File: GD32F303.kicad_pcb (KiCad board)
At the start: 2 copper layers, 0 parts

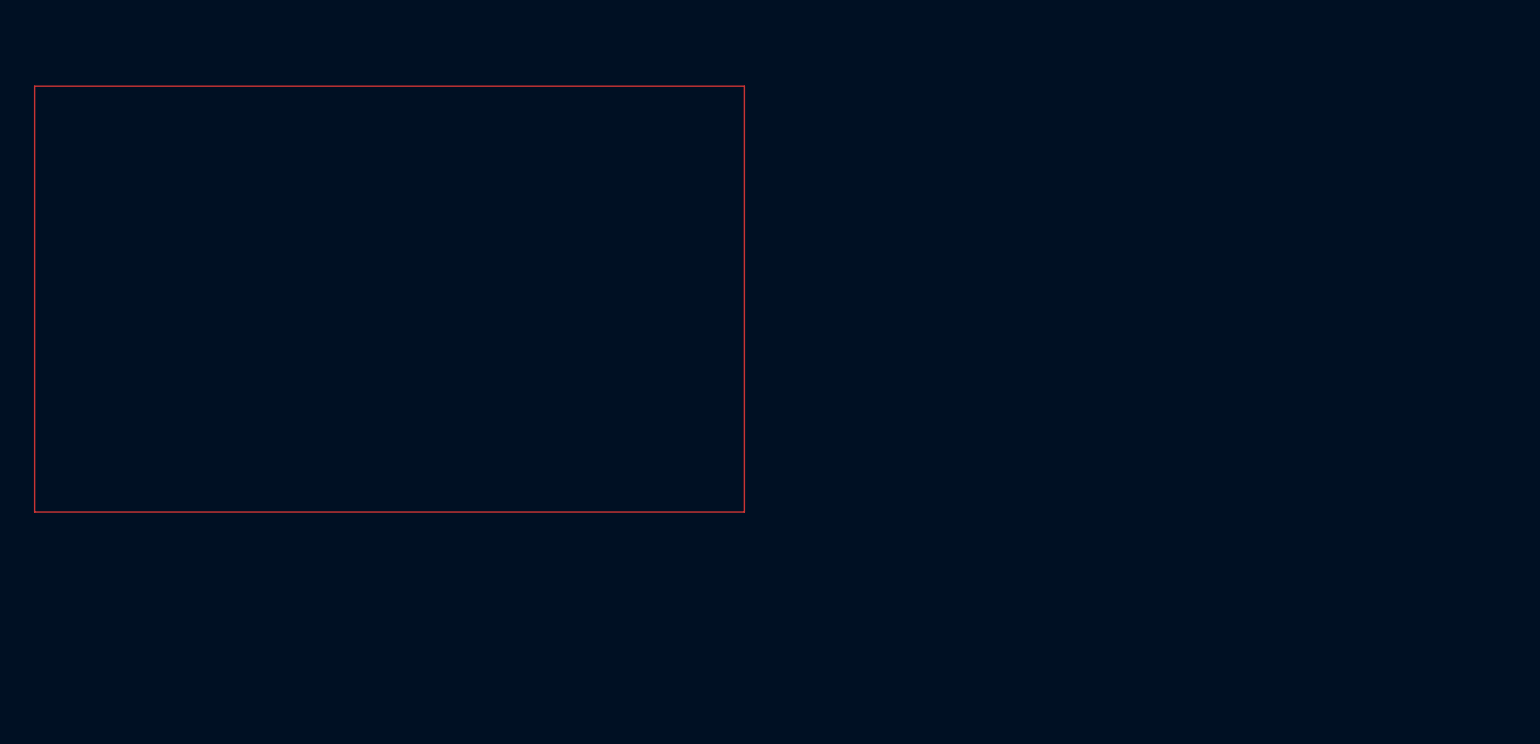
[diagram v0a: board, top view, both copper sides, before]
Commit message: 完成GD32F303控制板原理图与PCB设计
- 更新电源、CAN、RS232、RS485及电机通信子电路
- 切换并完善GD32F303VCT6核心原理图
- 新增PCB布局及所需符号、封装库文件
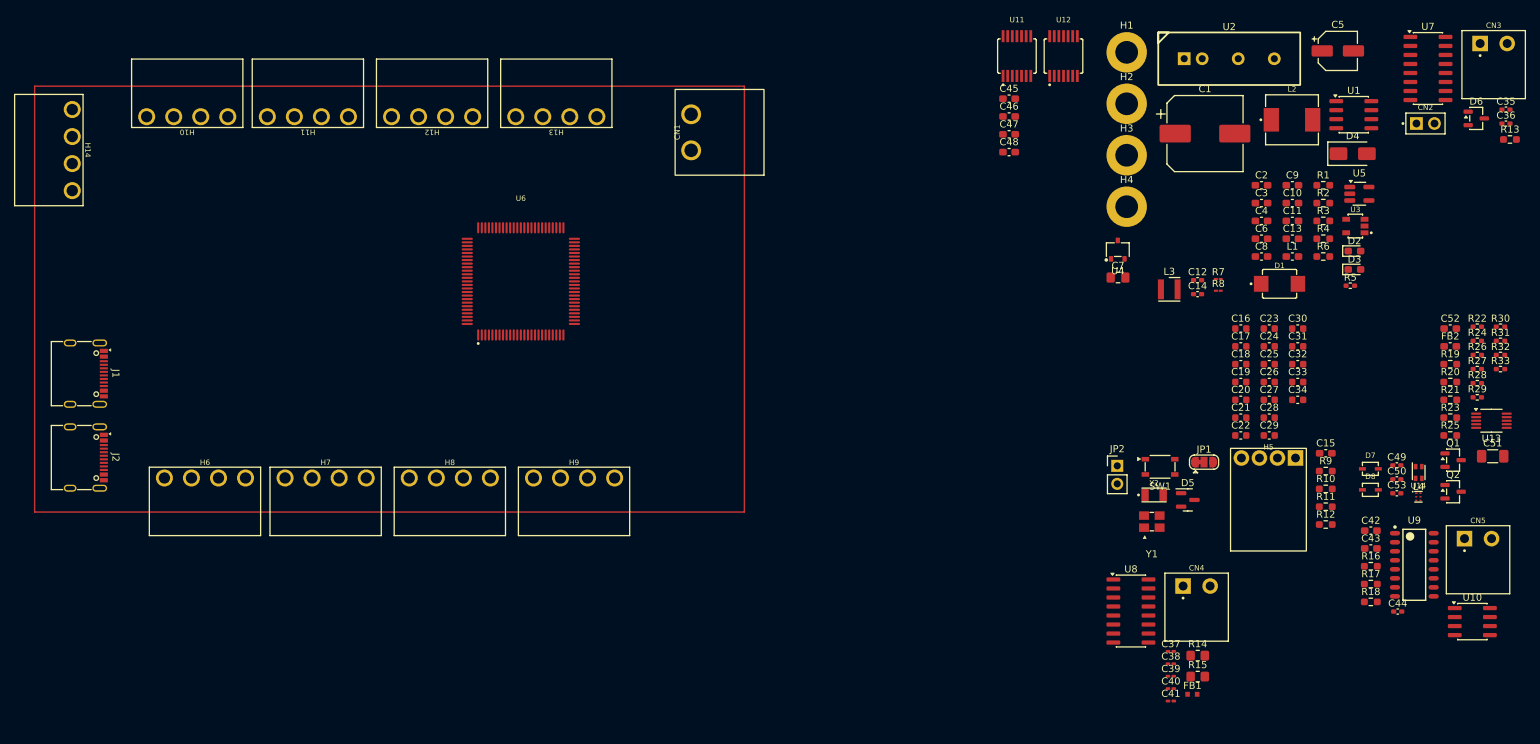
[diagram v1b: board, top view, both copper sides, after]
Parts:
- added C1: 470µF, Capacitor_SMD:CP_Elec_10x10.5, F.Cu at (250.4, 65.7)
- added C10: 100nF, Capacitor_SMD:C_0603_1608Metric_Pad1.08x0.95mm_HandSolder, F.Cu at (262.7, 75.5)
- added C11: 1nF, Capacitor_SMD:C_0603_1608Metric_Pad1.08x0.95mm_HandSolder, F.Cu at (262.7, 78.0)
- added C12: 100nF, Capacitor_SMD:C_0402_1005Metric_Pad0.74x0.62mm_HandSolder, F.Cu at (249.4, 86.3)
- added C13: 22uF, Capacitor_SMD:C_0603_1608Metric_Pad1.08x0.95mm_HandSolder, F.Cu at (262.7, 80.5)
- added C14: 100nF, Capacitor_SMD:C_0402_1005Metric_Pad0.74x0.62mm_HandSolder, F.Cu at (249.4, 88.3)
- added C15: 22pF, Capacitor_SMD:C_0603_1608Metric_Pad1.08x0.95mm_HandSolder, F.Cu at (267.4, 110.7)
- added C16: 100nF, Capacitor_SMD:C_0603_1608Metric, F.Cu at (255.4, 93.2)
- added C17: 100nF, Capacitor_SMD:C_0603_1608Metric, F.Cu at (255.4, 95.7)
- added C18: 100nF, Capacitor_SMD:C_0603_1608Metric, F.Cu at (255.4, 98.2)
- added C19: 100nF, Capacitor_SMD:C_0603_1608Metric, F.Cu at (255.4, 100.7)
- added C2: 10uF, Capacitor_SMD:C_0603_1608Metric_Pad1.08x0.95mm_HandSolder, F.Cu at (258.4, 73.0)
- added C20: 22pF, Capacitor_SMD:C_0603_1608Metric, F.Cu at (255.4, 103.2)
- added C21: 100nF, Capacitor_SMD:C_0603_1608Metric, F.Cu at (255.4, 105.7)
- added C22: 100nF, Capacitor_SMD:C_0603_1608Metric, F.Cu at (255.4, 108.2)
- added C23: 100nF, Capacitor_SMD:C_0603_1608Metric, F.Cu at (259.5, 93.2)
- added C24: 100nF, Capacitor_SMD:C_0603_1608Metric, F.Cu at (259.5, 95.7)
- added C25: 100nF, Capacitor_SMD:C_0603_1608Metric, F.Cu at (259.5, 98.2)
- added C26: 100nF, Capacitor_SMD:C_0603_1608Metric, F.Cu at (259.5, 100.7)
- added C27: 100nF, Capacitor_SMD:C_0603_1608Metric, F.Cu at (259.5, 103.2)
- added C28: 12pF, Capacitor_SMD:C_0603_1608Metric, F.Cu at (259.5, 105.7)
- added C29: 100nF, Capacitor_SMD:C_0603_1608Metric, F.Cu at (259.5, 108.2)
- added C3: 22pF, Capacitor_SMD:C_0603_1608Metric_Pad1.08x0.95mm_HandSolder, F.Cu at (258.4, 75.5)
- added C30: 100nF, Capacitor_SMD:C_0603_1608Metric, F.Cu at (263.5, 93.2)
- added C31: 12pF, Capacitor_SMD:C_0603_1608Metric, F.Cu at (263.5, 95.7)
- added C32: 100nF, Capacitor_SMD:C_0603_1608Metric, F.Cu at (263.5, 98.2)
- added C33: 10uF, Capacitor_SMD:C_0603_1608Metric, F.Cu at (263.5, 100.7)
- added C34: 100nF, Capacitor_SMD:C_0603_1608Metric, F.Cu at (263.5, 103.2)
- added C35: 100nF, Capacitor_SMD:C_0402_1005Metric_Pad0.74x0.62mm_HandSolder, F.Cu at (292.8, 62.3)
- added C36: 100nF, Capacitor_SMD:C_0402_1005Metric_Pad0.74x0.62mm_HandSolder, F.Cu at (292.8, 64.3)
- added C37: 100nF, Capacitor_SMD:C_0201_0603Metric_Pad0.64x0.40mm_HandSolder, F.Cu at (245.6, 138.6)
- added C38: 100nF, Capacitor_SMD:C_0201_0603Metric_Pad0.64x0.40mm_HandSolder, F.Cu at (245.6, 140.4)
- added C39: 100nF, Capacitor_SMD:C_0201_0603Metric_Pad0.64x0.40mm_HandSolder, F.Cu at (245.6, 142.1)
- added C4: 10uF, Capacitor_SMD:C_0603_1608Metric_Pad1.08x0.95mm_HandSolder, F.Cu at (258.4, 78.0)
- added C40: 100nF, Capacitor_SMD:C_0201_0603Metric_Pad0.64x0.40mm_HandSolder, F.Cu at (245.6, 143.9)
- added C41: 100nF, Capacitor_SMD:C_0201_0603Metric_Pad0.64x0.40mm_HandSolder, F.Cu at (245.6, 145.6)
- added C42: 0.1uF, Capacitor_SMD:C_0603_1608Metric_Pad1.08x0.95mm_HandSolder, F.Cu at (273.8, 121.6)
- added C43: 0.1uF, Capacitor_SMD:C_0603_1608Metric_Pad1.08x0.95mm_HandSolder, F.Cu at (273.8, 124.1)
- added C44: 100nF, Capacitor_SMD:C_0402_1005Metric_Pad0.74x0.62mm_HandSolder, F.Cu at (277.6, 133.0)
- added C45: 0.1uF, Capacitor_SMD:C_0603_1608Metric_Pad1.08x0.95mm_HandSolder, F.Cu at (222.8, 60.8)
- added C46: 0.1uF, Capacitor_SMD:C_0603_1608Metric_Pad1.08x0.95mm_HandSolder, F.Cu at (222.8, 63.3)
- added C47: 0.1uF, Capacitor_SMD:C_0603_1608Metric_Pad1.08x0.95mm_HandSolder, F.Cu at (222.8, 65.8)
- added C48: 0.1uF, Capacitor_SMD:C_0603_1608Metric_Pad1.08x0.95mm_HandSolder, F.Cu at (222.8, 68.3)
- added C49: 100nF, Capacitor_SMD:C_0402_1005Metric_Pad0.74x0.62mm_HandSolder, F.Cu at (277.4, 112.4)
- added C5: 220µF, Capacitor_SMD:CP_Elec_5x5.4, F.Cu at (269.1, 54.0)
- added C50: 100nF, Capacitor_SMD:C_0402_1005Metric_Pad0.74x0.62mm_HandSolder, F.Cu at (277.4, 114.4)
- added C51: 1nF, Capacitor_SMD:C_1206_3216Metric_Pad1.33x1.80mm_HandSolder, F.Cu at (290.9, 111.1)
- added C52: 10uF, Capacitor_SMD:C_0603_1608Metric_Pad1.08x0.95mm_HandSolder, F.Cu at (285.0, 93.2)
- added C53: 100nF, Capacitor_SMD:C_0402_1005Metric_Pad0.74x0.62mm_HandSolder, F.Cu at (277.4, 116.4)
- added C6: 10uF, Capacitor_SMD:C_0603_1608Metric_Pad1.08x0.95mm_HandSolder, F.Cu at (258.4, 80.5)
- added C7: 10uF, Capacitor_SMD:C_0805_2012Metric_Pad1.18x1.45mm_HandSolder, F.Cu at (238.1, 86.0)
- added C8: 1uF, Capacitor_SMD:C_0603_1608Metric_Pad1.08x0.95mm_HandSolder, F.Cu at (258.4, 83.0)
- added C9: 10uF, Capacitor_SMD:C_0603_1608Metric_Pad1.08x0.95mm_HandSolder, F.Cu at (262.7, 73.0)
- added CN1: DB2ERC-5.08-2P-GN, kicad_api_lib:DB2ERC-5.08-2P-GN, F.Cu at (178.0, 65.5)
- added CN2: PZ254-1-02-W-8.5, kicad_api_lib:PZ254-1-02-W-8.5, F.Cu at (281.5, 64.3)
- added CN3: WJ15EDGRC-3.81-2P, kicad_api_lib:WJ15EDGRC-3.81-2P, F.Cu at (291.1, 53.0)
- added CN4: WJ15EDGRC-3.81-2P, kicad_api_lib:WJ15EDGRC-3.81-2P, F.Cu at (249.2, 129.4)
- added CN5: WJ15EDGRC-3.81-2P, kicad_api_lib:WJ15EDGRC-3.81-2P, F.Cu at (288.9, 122.7)
- added D1: SMBJ24A, kicad_api_lib:SMBJ24A, F.Cu at (260.9, 86.8)
- added D2: LED, LED_SMD:LED_0603_1608Metric_Pad1.05x0.95mm_HandSolder, F.Cu at (271.5, 82.2)
- added D3: LED, LED_SMD:LED_0603_1608Metric_Pad1.05x0.95mm_HandSolder, F.Cu at (271.5, 84.8)
- added D4: SS34, Diode_SMD:D_SMA, F.Cu at (271.2, 68.5)
- added D5: BAT54CTA, kicad_api_lib:BAT54CTA, F.Cu at (248.0, 117.3)
- added D6: ESDA6V1L, Package_TO_SOT_SMD:SOT-23-3, F.Cu at (288.6, 63.5)
- added D7: SD03C, kicad_api_lib:SD03C, F.Cu at (273.7, 112.9)
- added D8: SD03C, kicad_api_lib:SD03C, F.Cu at (273.7, 115.9)
- added FB1: BLM18AG601SN1D, kicad_api_lib:BLM18AG601SN1D, F.Cu at (248.6, 144.7)
- added FB2: 100ohm@100MHz, Capacitor_SMD:C_0603_1608Metric_Pad1.08x0.95mm_HandSolder, F.Cu at (285.0, 95.7)
- added H1: MountingHole_Pad, MountingHole:MountingHole_3.2mm_M3_ISO7380_Pad, F.Cu at (239.4, 54.2)
- added H10: KF2EDGRM-3.81-4P, kicad_api_lib:KF2EDGRM-3.81-4P, F.Cu at (107.0, 63.3)
- added H11: KF2EDGRM-3.81-4P, kicad_api_lib:KF2EDGRM-3.81-4P, F.Cu at (124.0, 63.3)
- added H12: KF2EDGRM-3.81-4P, kicad_api_lib:KF2EDGRM-3.81-4P, F.Cu at (141.5, 63.3)
- added H13: KF2EDGRM-3.81-4P, kicad_api_lib:KF2EDGRM-3.81-4P, F.Cu at (159.0, 63.3)
- added H14: KF2EDGRM-3.81-4P, kicad_api_lib:KF2EDGRM-3.81-4P, F.Cu at (90.8, 68.0)
- added H2: MountingHole_Pad, MountingHole:MountingHole_3.2mm_M3_ISO7380_Pad, F.Cu at (239.4, 61.5)
- added H3: MountingHole_Pad, MountingHole:MountingHole_3.2mm_M3_ISO7380_Pad, F.Cu at (239.4, 68.7)
- added H4: MountingHole_Pad, MountingHole:MountingHole_3.2mm_M3_ISO7380_Pad, F.Cu at (239.4, 76.0)
- added H5: X9254WR-04-N0SN, kicad_api_lib:X9254WR-04-N0SN, F.Cu at (259.3, 111.4)
- added H6: KF2EDGRM-3.81-4P, kicad_api_lib:KF2EDGRM-3.81-4P, F.Cu at (109.5, 114.2)
- added H7: KF2EDGRM-3.81-4P, kicad_api_lib:KF2EDGRM-3.81-4P, F.Cu at (126.5, 114.2)
- added H8: KF2EDGRM-3.81-4P, kicad_api_lib:KF2EDGRM-3.81-4P, F.Cu at (144.0, 114.2)
- added H9: KF2EDGRM-3.81-4P, kicad_api_lib:KF2EDGRM-3.81-4P, F.Cu at (161.5, 114.2)
- added J1: TYPE-C-31-M-31, kicad_api_lib:TYPE-C 16PIN 2MD(073), F.Cu at (94.2, 99.5)
- added J2: TYPE-C 16PIN 2MD(073), kicad_api_lib:TYPE-C 16PIN 2MD(073), F.Cu at (94.2, 111.3)
- added JP1: SolderJumper_3_Bridged12, Jumper:SolderJumper-3_P1.3mm_Bridged12_RoundedPad1.0x1.5mm, F.Cu at (250.3, 112.0)
- added JP2: Jumper_2_Small_Open, Connector_PinHeader_2.54mm:PinHeader_1x02_P2.54mm_Vertical, F.Cu at (238.0, 112.5)
- added L1: 1uF, Capacitor_SMD:C_0603_1608Metric_Pad1.08x0.95mm_HandSolder, F.Cu at (262.7, 83.0)
- added L2: SMMS0650-680M, kicad_api_lib:SMMS0650-680M, F.Cu at (262.7, 63.7)
- added L3: 2.2uH, Inductor_SMD_Wurth:L_Wurth_WE-LQSH-3012, F.Cu at (245.4, 87.6)
- added L4: PCAQ2012B-900T040, Inductor_SMD:L_CommonModeChoke_Coilcraft_0805USB, F.Cu at (280.5, 113.4)
- added Q1: CJ3134K KF, Package_TO_SOT_SMD:SOT-23-3, F.Cu at (285.4, 111.7)
- added Q2: CJ3134K KF, Package_TO_SOT_SMD:SOT-23-3, F.Cu at (285.4, 116.1)
- added R1: 10k, Resistor_SMD:R_0603_1608Metric_Pad0.98x0.95mm_HandSolder, F.Cu at (267.1, 73.0)
- added R10: 1MΩ, Resistor_SMD:R_0603_1608Metric_Pad0.98x0.95mm_HandSolder, F.Cu at (267.4, 115.7)
- added R11: 10kΩ, Resistor_SMD:R_0603_1608Metric_Pad0.98x0.95mm_HandSolder, F.Cu at (267.4, 118.2)
- added R12: 10kΩ, Resistor_SMD:R_0603_1608Metric_Pad0.98x0.95mm_HandSolder, F.Cu at (267.4, 120.8)
- added R13: 120, Resistor_SMD:R_0603_1608Metric_Pad0.98x0.95mm_HandSolder, F.Cu at (293.4, 66.5)
- added R14: 22, Resistor_SMD:R_0805_2012Metric_Pad1.20x1.40mm_HandSolder, F.Cu at (249.4, 139.2)
- added R15: 100, Resistor_SMD:R_0805_2012Metric_Pad1.20x1.40mm_HandSolder, F.Cu at (249.4, 142.2)
- added R16: 10K, Resistor_SMD:R_0603_1608Metric_Pad0.98x0.95mm_HandSolder, F.Cu at (273.8, 126.6)
- added R17: 120, Resistor_SMD:R_0603_1608Metric_Pad0.98x0.95mm_HandSolder, F.Cu at (273.8, 129.2)
- added R18: 10K, Resistor_SMD:R_0603_1608Metric_Pad0.98x0.95mm_HandSolder, F.Cu at (273.8, 131.7)
- added R19: 0, Resistor_SMD:R_0603_1608Metric_Pad0.98x0.95mm_HandSolder, F.Cu at (285.0, 98.2)
- added R2: 10k, Resistor_SMD:R_0603_1608Metric_Pad0.98x0.95mm_HandSolder, F.Cu at (267.1, 75.5)
- added R20: 0, Resistor_SMD:R_0603_1608Metric_Pad0.98x0.95mm_HandSolder, F.Cu at (285.0, 100.7)
- added R21: 0, Resistor_SMD:R_0603_1608Metric_Pad0.98x0.95mm_HandSolder, F.Cu at (285.0, 103.2)
- added R22: 4.7K, Resistor_SMD:R_0402_1005Metric_Pad0.72x0.64mm_HandSolder, F.Cu at (288.8, 92.9)
- added R23: 0, Resistor_SMD:R_0603_1608Metric_Pad0.98x0.95mm_HandSolder, F.Cu at (285.0, 105.7)
- added R24: 4.7K, Resistor_SMD:R_0402_1005Metric_Pad0.72x0.64mm_HandSolder, F.Cu at (288.8, 94.9)
- added R25: 0, Resistor_SMD:R_0603_1608Metric_Pad0.98x0.95mm_HandSolder, F.Cu at (285.0, 108.2)
- added R26: 5.1K, Resistor_SMD:R_0402_1005Metric_Pad0.72x0.64mm_HandSolder, F.Cu at (288.8, 96.9)
- added R27: 5.1K, Resistor_SMD:R_0402_1005Metric_Pad0.72x0.64mm_HandSolder, F.Cu at (288.8, 98.9)
- added R28: 4.7K, Resistor_SMD:R_0402_1005Metric_Pad0.72x0.64mm_HandSolder, F.Cu at (288.8, 100.8)
- added R29: 4.7K, Resistor_SMD:R_0402_1005Metric_Pad0.72x0.64mm_HandSolder, F.Cu at (288.8, 102.8)
- added R3: 22.1k, Resistor_SMD:R_0603_1608Metric_Pad0.98x0.95mm_HandSolder, F.Cu at (267.1, 78.0)
- added R30: 22, Resistor_SMD:R_0402_1005Metric_Pad0.72x0.64mm_HandSolder, F.Cu at (292.0, 92.9)
- added R31: 22, Resistor_SMD:R_0402_1005Metric_Pad0.72x0.64mm_HandSolder, F.Cu at (292.0, 94.9)
- added R32: 5.1K, Resistor_SMD:R_0402_1005Metric_Pad0.72x0.64mm_HandSolder, F.Cu at (292.0, 96.9)
- added R33: 5.1K, Resistor_SMD:R_0402_1005Metric_Pad0.72x0.64mm_HandSolder, F.Cu at (292.0, 98.9)
- added R4: 100k, Resistor_SMD:R_0603_1608Metric_Pad0.98x0.95mm_HandSolder, F.Cu at (267.1, 80.5)
- added R5: 10K, Resistor_SMD:R_0402_1005Metric_Pad0.72x0.64mm_HandSolder, F.Cu at (270.9, 87.1)
- added R6: 1M, Resistor_SMD:R_0603_1608Metric_Pad0.98x0.95mm_HandSolder, F.Cu at (267.1, 83.0)
- added R7: 100K, Resistor_SMD:R_01005_0402Metric_Pad0.57x0.30mm_HandSolder, F.Cu at (252.3, 86.2)
- added R8: 22K, Resistor_SMD:R_01005_0402Metric_Pad0.57x0.30mm_HandSolder, F.Cu at (252.3, 87.8)
- added R9: 10kΩ, Resistor_SMD:R_0603_1608Metric_Pad0.98x0.95mm_HandSolder, F.Cu at (267.4, 113.2)
- added SW1: SKRPACE010, kicad_api_lib:SKRPACE010, F.Cu at (244.1, 112.6)
- added U1: XL1509-5.0, Package_SO:SOIC-8_3.9x4.9mm_P1.27mm, F.Cu at (271.4, 63.0)
- added U10: SIT3485ESA, Package_SO:SOIC-8_3.9x4.9mm_P1.27mm, F.Cu at (288.1, 134.4)
- added U11: TXS0104EPWR, kicad_api_lib:TXS0104EPWR, F.Cu at (223.9, 54.8)
- added U12: TXS0104EPWR, kicad_api_lib:TXS0104EPWR, F.Cu at (230.5, 54.8)
- added U13: CH340E, kicad_api_lib:CH340E, F.Cu at (290.8, 106.1)
- added U14: TPD4S012DRYR, Package_DFN_QFN:TPD4S012DRYR, F.Cu at (280.5, 116.8)
- added U2: B0503S-2WR3L, Converter_DCDC:B0503S-2WR3L, F.Cu at (247.5, 55.1)
- added U3: SY8089A1AAC, kicad_api_lib:SY8089A1AAC, F.Cu at (271.6, 78.7)
- added U4: CH213K, kicad_api_lib:CH213K, F.Cu at (238.1, 82.0)
- added U5: SY8089AAC, Package_TO_SOT_SMD:SOT-23-5_HandSoldering, F.Cu at (272.1, 74.2)
- added U6: GD32F303VCT6, kicad_api_lib:GD32F303VCT6, F.Cu at (154.0, 86.5)
- added U7: ISO1050DWR, Package_SO:SOIC-16_3.9x9.9mm_P1.27mm, F.Cu at (281.8, 56.5)
- added U8: SP3232EEN-L/TR, Package_SO:SOIC-16_3.9x9.9mm_P1.27mm, F.Cu at (240.0, 132.9)
- added U9: π131U30, kicad_api_lib:π131U30, F.Cu at (279.9, 126.4)
- added Y1: TAXM8M4RDBCCT2T, kicad_api_lib:TAXM8M4RDBCCT2T, F.Cu at (242.9, 120.3)
- added Y2: XKXGI-SUA-32.768K, kicad_api_lib:XKXGI-SUA-32.768K, F.Cu at (243.2, 116.6)

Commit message: 优化接口原理图与PCB布局
- 精简CAN接口并调整各子页器件编号
- 更新电源输入端子与Type-C接口封装
- 重新整理控制板PCB器件布局
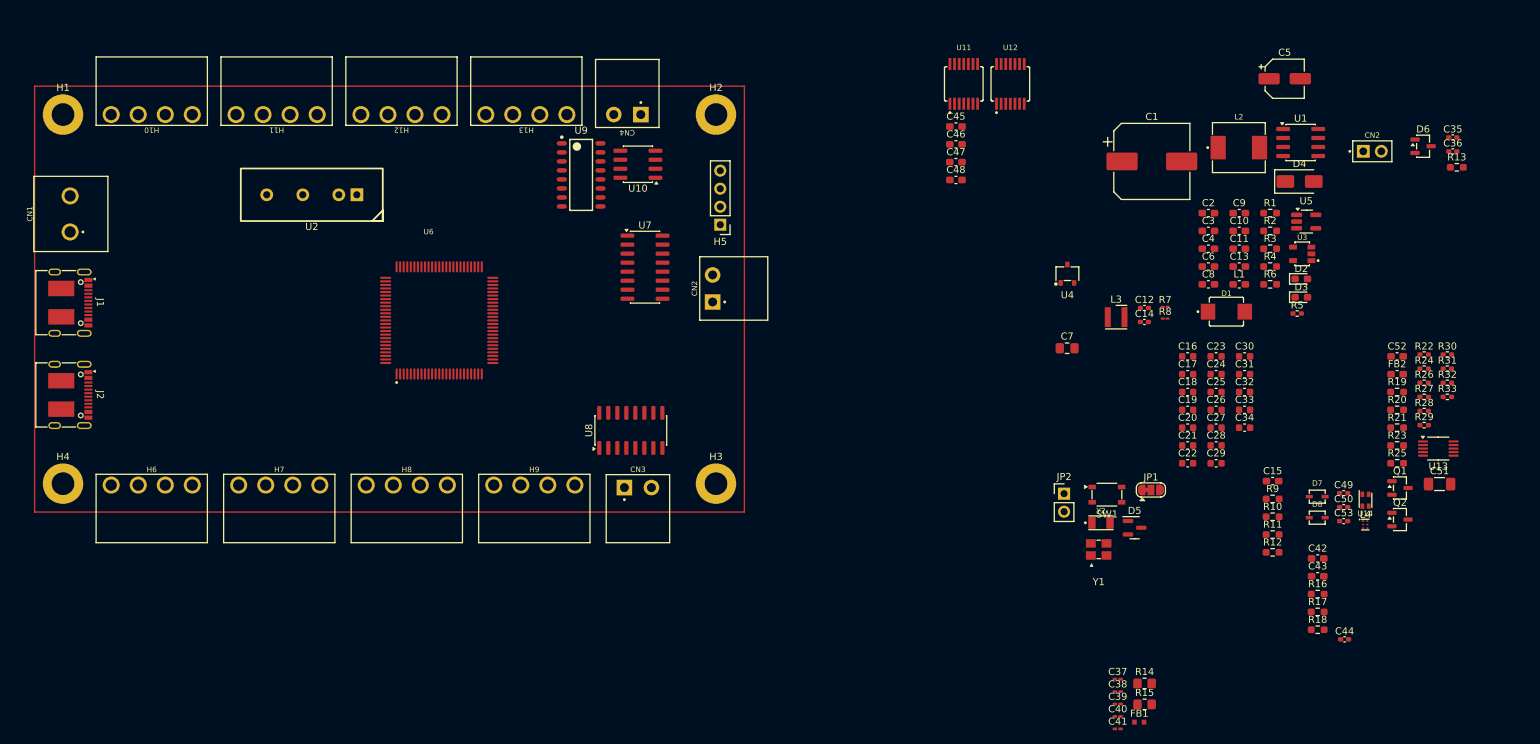
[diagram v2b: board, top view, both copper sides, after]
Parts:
- removed H14: KF2EDGRM-3.81-4P, kicad_api_lib:KF2EDGRM-3.81-4P
- CN1: value DB2ERC-5.08-2P-GN -> KF128L-5.08-2P; footprint kicad_api_lib:DB2ERC-5.08-2P-GN -> kicad_api_lib:KF128L-5.08-2P
- H5: footprint kicad_api_lib:X9254WR-04-N0SN -> Connector_PinHeader_2.54mm:PinHeader_1x04_P2.54mm_Vertical
- J1, J2: footprint kicad_api_lib:TYPE-C 16PIN 2MD(073) -> kicad_api_lib:TYPE-C 16PIN 2MD NEW(073)
- moved H4 154.9 mm to (89.5, 115.0)
- moved H1 150.1 mm to (89.5, 63.0)
- moved U10 134.1 mm to (170.5, 70.0), turned to 180 degrees
- moved CN4 133.9 mm to (169.0, 63.0), turned to 180 degrees
- moved U9 129.6 mm to (162.5, 71.5)
- moved U2 118.1 mm to (130.9, 74.3), turned to 180 degrees
- moved CN2 115.3 mm to (181.0, 87.5), turned to 90 degrees
- moved U7 113.8 mm to (171.5, 84.5)
- moved CN1 88.3 mm to (90.5, 77.0)
- moved H5 83.9 mm to (182.1, 78.5), turned to 180 degrees
- moved CN3 79.9 mm to (170.5, 115.5)
- moved U8 74.9 mm to (169.5, 107.5), turned to 90 degrees
- moved H3 74.1 mm to (181.5, 115.0)
- moved H2 57.9 mm to (181.5, 63.0)
- moved U6 12.7 mm to (142.5, 92.0)
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- renumbered CN3 to CN2, CN4 to CN3, CN5 to CN4
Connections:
- R13 pad 2: Net-(CN2-Pad2) -> /CAN/CANH

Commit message: 完善PCB布线与接口电源网络
- 调整控制板PCB器件布局与走线
- 更新MCU、电源及通信接口原理图
- 统一隔离接口地和电源网络标签并修正封装属性
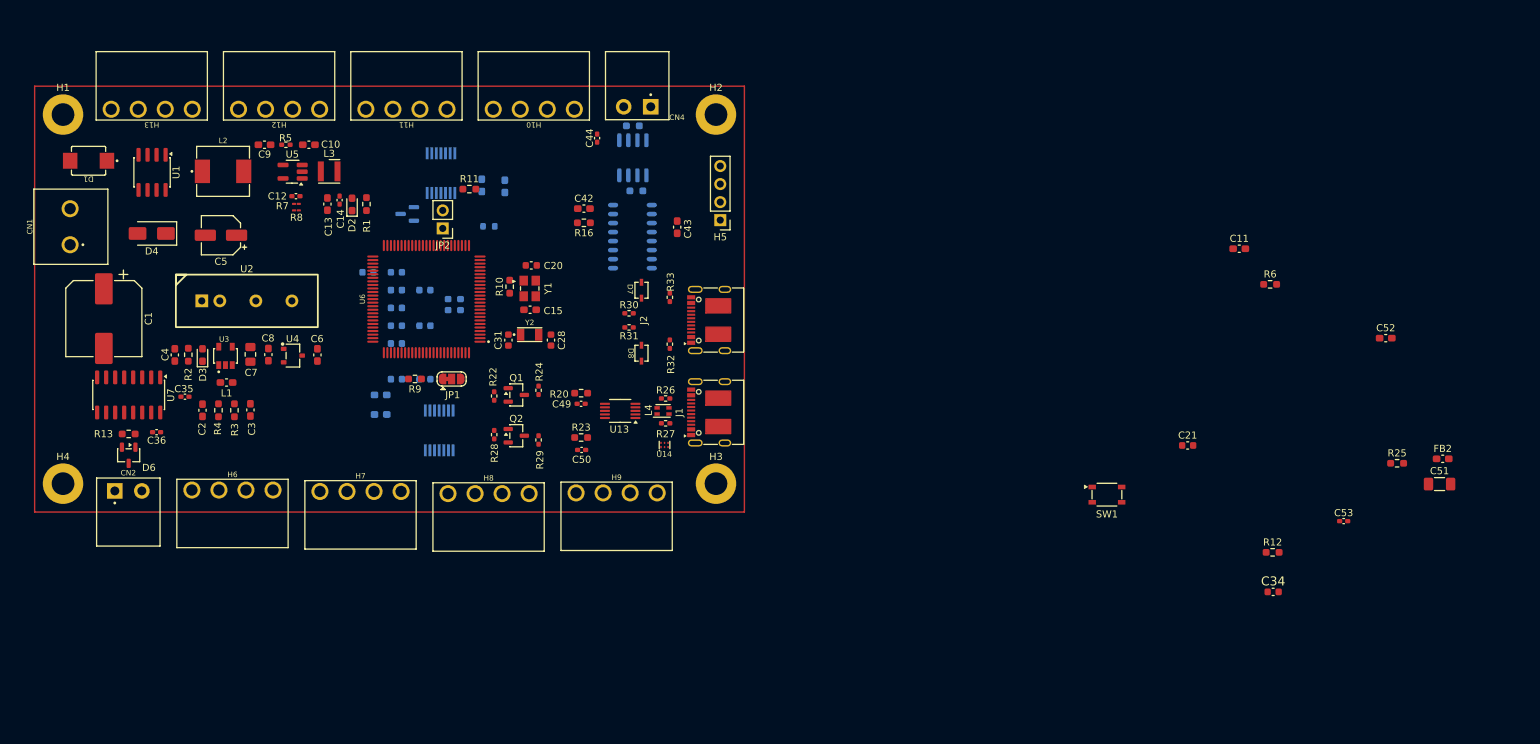
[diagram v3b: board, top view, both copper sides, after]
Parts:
- removed C32: 100nF, Capacitor_SMD:C_0603_1608Metric
- removed C33: 10uF, Capacitor_SMD:C_0603_1608Metric
- removed C37, C38, C39, C40, C41: 100nF, Capacitor_SMD:C_0201_0603Metric_Pad0.64x0.40mm_HandSolder
- removed the CN2 at (274.0, 68.2)
- removed CN3: WJ15EDGRC-3.81-2P, kicad_api_lib:WJ15EDGRC-3.81-2P
- removed FB1: BLM18AG601SN1D, kicad_api_lib:BLM18AG601SN1D
- removed R14: 22, Resistor_SMD:R_0805_2012Metric_Pad1.20x1.40mm_HandSolder
- removed R15: 100, Resistor_SMD:R_0805_2012Metric_Pad1.20x1.40mm_HandSolder
- removed R19, R21: 0, Resistor_SMD:R_0603_1608Metric_Pad0.98x0.95mm_HandSolder
- removed U8: SP3232EEN-L/TR, Package_SO:SOIC-16_3.9x9.9mm_P1.27mm
- added B01: VBAT_BAT, Resistor_SMD:R_0603_1608Metric, B.Cu at (149.5, 78.8)
- C16, C17, C18, C19, C22, C23, C24, C25, C26, C27, C29, C30, C45, C46, C47, C48, D5, R17, R18, U10, U11, U12, U9: moved to B.Cu
- moved R13 190.9 mm to (98.8, 108.0)
- moved D6 187.5 mm to (98.8, 111.0), turned to -90 degrees
- moved C36 186.9 mm to (102.7, 107.8), turned to 180 degrees
- moved C35 182.3 mm to (106.7, 102.8), turned to 180 degrees
- moved D4 161.9 mm to (102.0, 79.8), turned to 180 degrees
- moved U1 161.9 mm to (102.0, 71.1), turned to -90 degrees
- moved D1 161.7 mm to (93.1, 69.5), turned to 180 degrees
- moved D3 155.0 mm to (109.2, 96.9), turned to 90 degrees
- moved R2 153.4 mm to (107.2, 96.8), turned to 90 degrees
- moved U3 152.4 mm to (112.4, 97.0), turned to -90 degrees
- moved C5 151.5 mm to (111.8, 80.0), turned to 180 degrees
- moved R4 149.6 mm to (111.4, 104.7), turned to 90 degrees
- moved C1 149.3 mm to (95.2, 91.8), turned to -90 degrees
- moved R3 147.7 mm to (113.7, 104.7), turned to -90 degrees
- moved C4 146.4 mm to (105.2, 96.9), turned to -90 degrees
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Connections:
- net DN renamed /MCU_Core/USB_TTL_CH340/DN
- net DP renamed /MCU_Core/USB_TTL_CH340/DP
- C28 pad 1: /MCU_Core/OSC32_OUT -> GND
- C28 pad 2: Net-(C28-Pad2) -> /MCU_Core/OSC32_OUT
- C31 pad 1: /MCU_Core/OSC32_IN -> GND
- C31 pad 2: Net-(C31-Pad2) -> /MCU_Core/OSC32_IN
- C35 pad 2: GNDS -> GND
- C44 pad 1: +3.3V_ISO -> +3V3_ISO
- CN4 pad 1: /RS485/RS485_B -> /RS485/RS485A
- CN4 pad 2: /RS485/RS485_A -> /RS485/RS485B
- D2 pad 2: +5V_ISO -> +3V3
- Q1 pad 3: CH_RX -> /MCU_Core/USB_TTL_CH340/CH_RX
- Q2 pad 3: CH_TX -> /MCU_Core/USB_TTL_CH340/CH_TX
- R17 pad 1: /RS485/RS485_A -> /RS485/RS485A
- R24 pad 2: CH_RX -> /MCU_Core/USB_TTL_CH340/CH_RX
- R25 pad 2: CH_RX -> /MCU_Core/USB_TTL_CH340/CH_TX
- R29 pad 2: CH_TX -> /MCU_Core/USB_TTL_CH340/CH_TX
- U10 pad 6: /RS485/RS485_A -> /RS485/RS485A
- U10 pad 8: +3.3V_ISO -> +3V3_ISO
- U13 pad 8: CH_TX -> /MCU_Core/USB_TTL_CH340/CH_RX
- U13 pad 9: CH_RX -> /MCU_Core/USB_TTL_CH340/CH_TX
- U7 pad 2: GNDS -> GND
- U7 pad 7: GNDS -> GND
- U7 pad 8: GNDS -> GND
- Y2 pad 1: Net-(C31-Pad2) -> /MCU_Core/OSC32_IN
- Y2 pad 2: Net-(C28-Pad2) -> /MCU_Core/OSC32_OUT
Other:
- copper layers 2 -> 4

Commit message: 保存商业化布局优化前工程版本
- 保存当前PCB布局与走线调整
- 更新MCU核心页器件属性
- 记录后续商业板布局优化前的可回退检查点
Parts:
- B01: footprint Resistor_SMD:R_0603_1608Metric -> Battery:BatteryHolder_Keystone_500; moved to F.Cu
- C21: moved to B.Cu
- moved C52 101.5 mm to (174.5, 99.5), turned to 180 degrees
- moved C21 99.0 mm to (149.5, 99.0)
- moved C53 97.4 mm to (174.5, 100.8), turned to 180 degrees
- moved C51 41.0 mm to (246.1, 98.2)
- moved FB2 32.9 mm to (253.1, 99.8)
- moved D5 27.6 mm to (154.6, 99.0)
- moved B01 23.9 mm to (162.3, 98.9), turned to 90 degrees
- moved C29 15.6 mm to (145.0, 87.2)
- moved C30 12.6 mm to (145.0, 83.8)
- moved C11 10.4 mm to (249.4, 90.5)
- moved R6 10.4 mm to (253.8, 95.5)
- moved C22 7.68 mm to (142.0, 92.8)
- moved C15 6.25 mm to (155.3, 84.2)
- moved C20 6.25 mm to (155.5, 78.0)
- moved C28 6.25 mm to (158.3, 88.5)
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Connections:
- B01 pad 1: GND -> VBAT
- D5 pad 2: GND -> VBAT
